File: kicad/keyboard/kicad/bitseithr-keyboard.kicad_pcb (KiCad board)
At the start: 4 copper layers, 419 x 206 mm, 100 parts, among them P2 KEYB CONN 1

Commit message: continued keyboard pcb
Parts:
- added U?: SW-TH_EC11E1820402, clholm-kicad-library:SW-TH_EC11E1820402, F.Cu at (396.5, 176.5)
- added U?: SW-TH_EC11E1820402, clholm-kicad-library:SW-TH_EC11E1820402, F.Cu at (396.5, 136.5)
- moved D31 258.1 mm to (136.1, 225.5)
- moved D34 258.1 mm to (136.1, 223.1)
- moved D36 258.1 mm to (135.3, 218.3)
- moved P2 256.3 mm to (93.3, 234.3)
- moved D37 154.4 mm to (208.0, 86.5)
- moved R16 140.5 mm to (209.0, 96.0)
- moved R15 124.3 mm to (220.0, 83.5)
- moved HOLE 7.00 mm to (192.0, 166.0)
- moved HOLE 4.47 mm to (110.0, 129.0)
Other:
- outline, holes or cut-outs redrawn

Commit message: updated control scheme layout
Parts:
- moved U? 121.1 mm to (303.0, 213.5), turned to 180 degrees
- moved U? 65.0 mm to (343.0, 213.5), turned to 180 degrees
- moved HOLE 4.00 mm to (444.5, 110.2)
- moved HOLE 4.00 mm to (294.5, 62.5)
- moved HOLE 4.00 mm to (194.5, 62.5)
- moved HOLE 4.00 mm to (94.5, 62.5)
- moved HOLE 4.00 mm to (444.5, 158.0)
- moved HOLE 4.00 mm to (444.5, 253.5)
- moved HOLE 4.00 mm to (344.5, 253.5)
- moved HOLE 4.00 mm to (244.5, 253.5)
- moved HOLE 4.00 mm to (444.5, 205.8)
- moved HOLE 4.00 mm to (144.5, 253.5)
- moved HOLE 4.00 mm to (344.5, 62.5)
- moved HOLE 4.00 mm to (144.5, 62.5)
- moved HOLE 4.00 mm to (244.5, 62.5)
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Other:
- board size 419 x 206 mm -> 415 x 206 mm

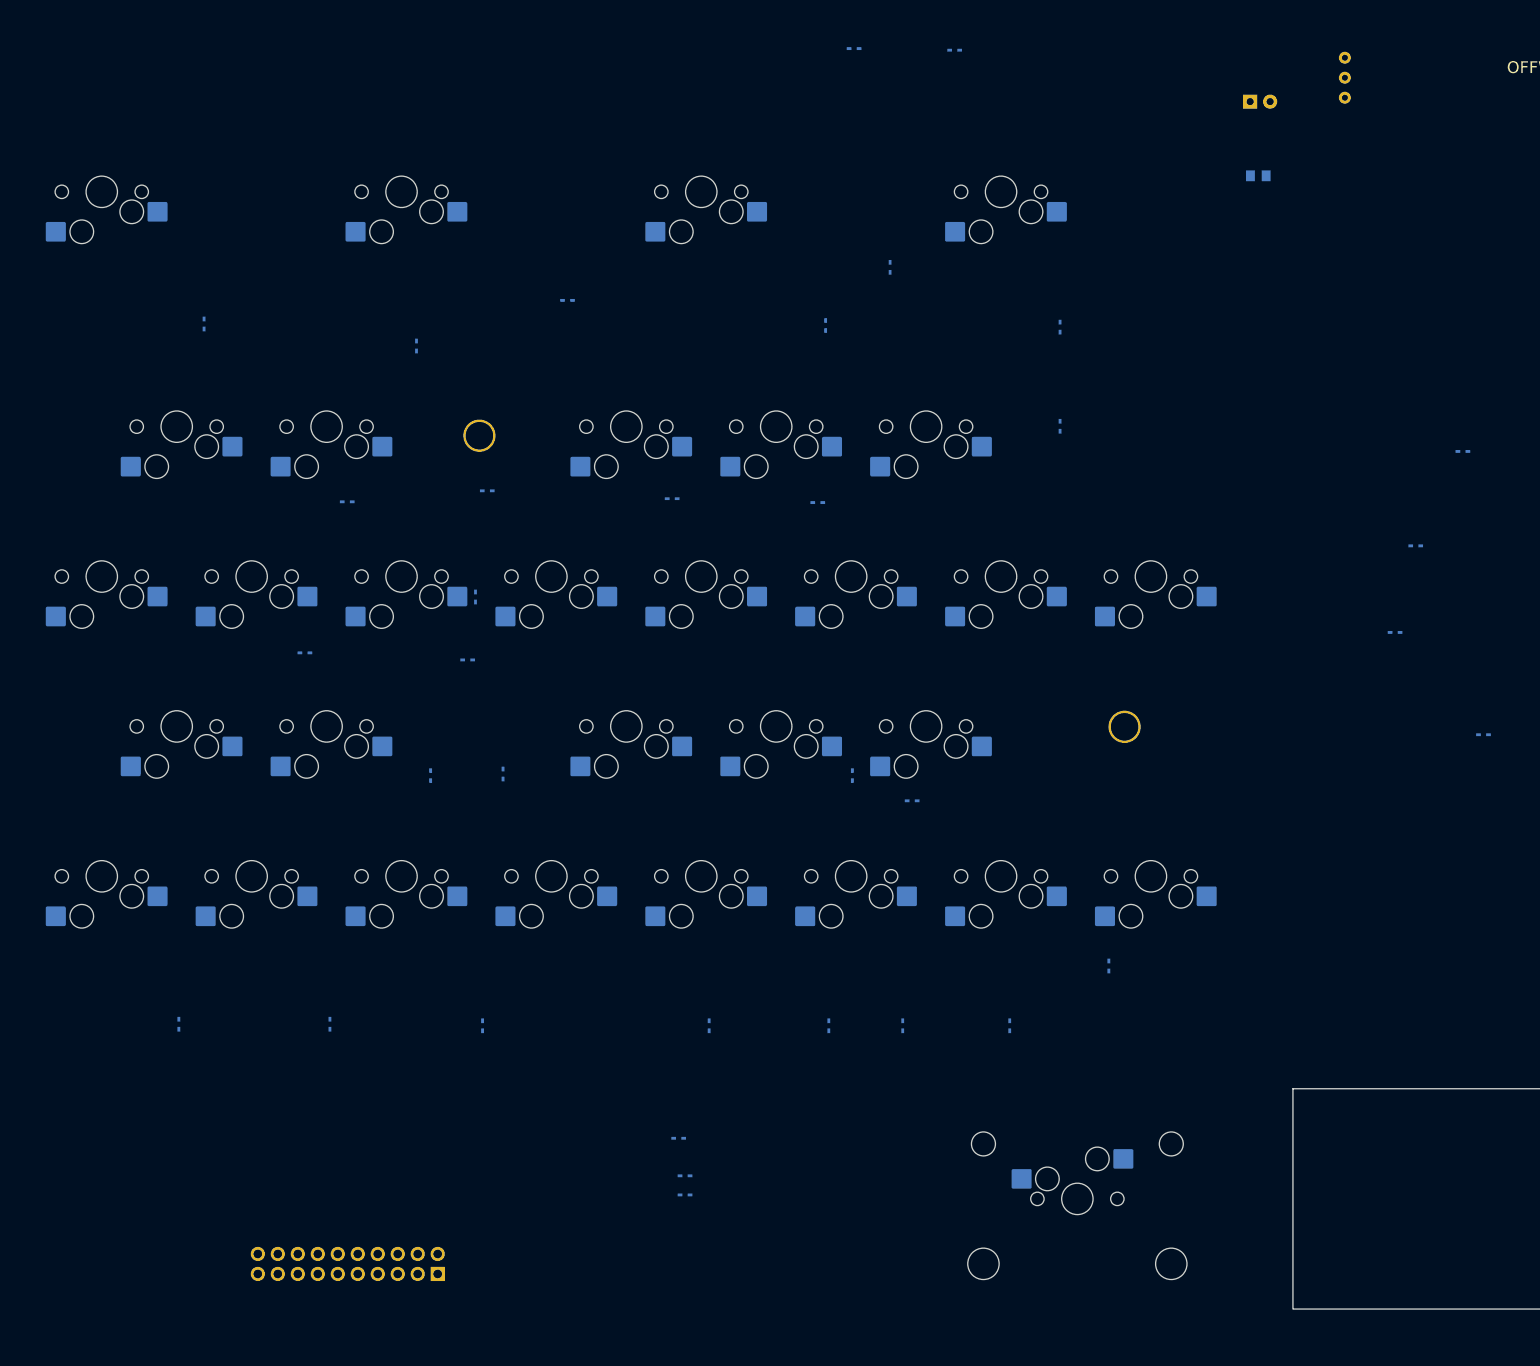
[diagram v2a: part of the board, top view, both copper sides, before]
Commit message: arranged diodes on board
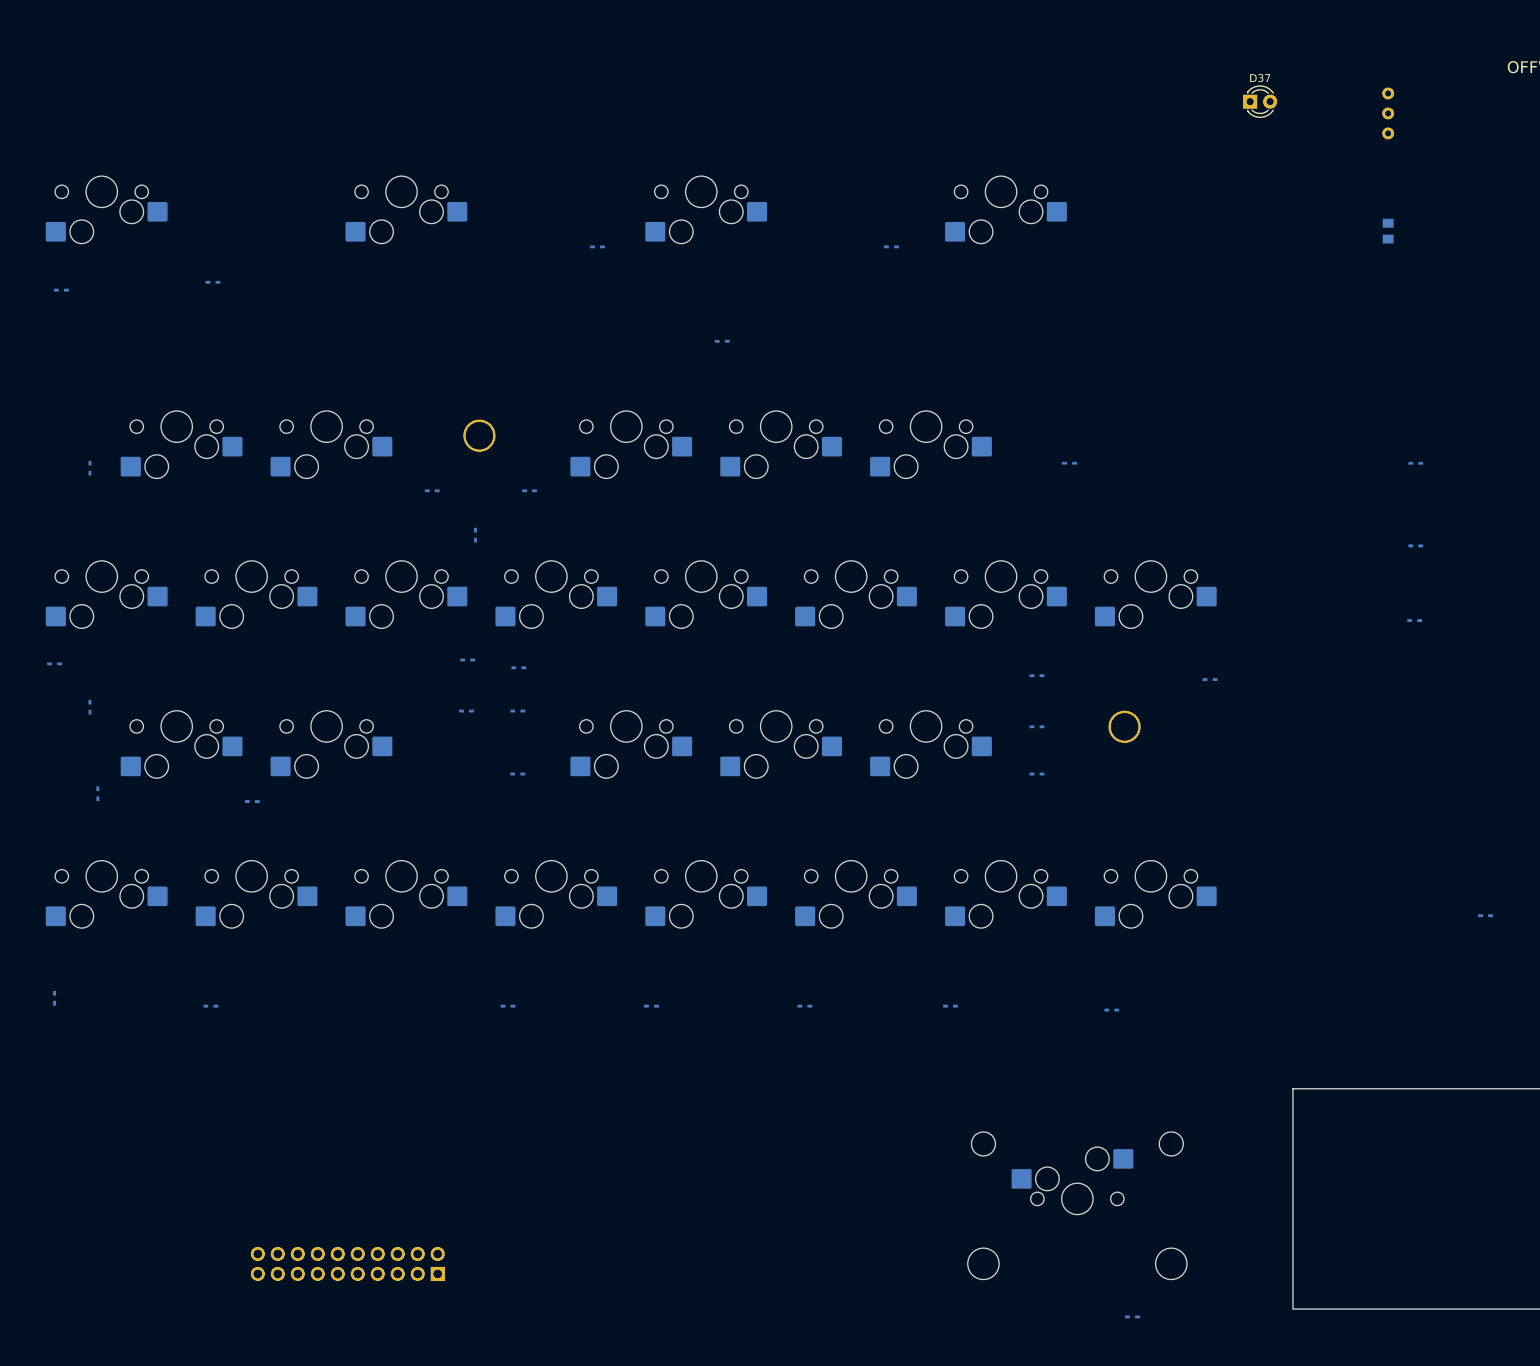
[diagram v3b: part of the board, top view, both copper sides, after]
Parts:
- D37: moved to F.Cu
- moved D16 165.0 mm to (193.0, 241.0)
- moved D25 123.0 mm to (151.4, 201.5), turned to 180 degrees
- moved D34 116.5 mm to (228.9, 152.5)
- moved D36 106.4 mm to (237.9, 190.0)
- moved D10 100.5 mm to (75.9, 201.5)
- moved D21 98.7 mm to (131.9, 201.5), turned to 0 degrees
- moved D6 94.8 mm to (56.0, 200.5), turned to 90 degrees
- moved D31 93.5 mm to (202.9, 160.0)
- moved D32 83.9 mm to (190.4, 202.0)
- moved D15 76.5 mm to (113.6, 201.5), turned to 0 degrees
- moved D30 76.0 mm to (169.9, 201.5), turned to 0 degrees
- moved D24 68.4 mm to (108.4, 164.0), turned to 0 degrees
- moved D12 68.3 mm to (104.0, 136.0), turned to 180 degrees
- moved D11 52.1 mm to (76.1, 109.5), turned to 0 degrees
- moved D14 51.5 mm to (115.0, 158.5), turned to 180 degrees
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
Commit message: shrank board length
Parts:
- moved D37 91.2 mm to (117.9, 72.0)
- moved HOLE 50.0 mm to (394.5, 110.2)
- moved HOLE 50.0 mm to (394.5, 158.0)
- moved HOLE 50.0 mm to (394.5, 253.5)
- moved HOLE 50.0 mm to (394.5, 205.8)
- moved HOLE 50.0 mm to (394.5, 62.5)
- moved HOLE 43.8 mm to (350.8, 253.5)
- moved HOLE 43.8 mm to (350.8, 62.5)
- moved HOLE 37.5 mm to (307.0, 253.5)
- moved HOLE 37.5 mm to (307.0, 62.5)
- moved HOLE 31.2 mm to (263.2, 62.5)
- moved HOLE 31.2 mm to (263.2, 253.5)
- moved HOLE 25.0 mm to (219.5, 253.5)
- moved HOLE 25.0 mm to (219.5, 62.5)
- moved HOLE 18.8 mm to (175.8, 62.5)
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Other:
- board size 415 x 206 mm -> 365 x 206 mm
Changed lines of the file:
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@@
 	(footprint "MountingHole:MountingHole_3.5mm"
 		(layer "F.Cu")
-		(at 444.5 110.25)
+		(at 394.5 110.25)
 		(property "Reference" "HOLE"
 			(at 0 -3.45 0)
@@
 	(footprint "MountingHole:MountingHole_3.5mm"
 		(layer "F.Cu")
-		(at 444.5 205.75)
+		(at 394.5 205.75)
 		(property "Reference" "HOLE"
 			(at 0 -3.45 0)
@@
 	(footprint "MountingHole:MountingHole_3.5mm"
 		(layer "F.Cu")
-		(at 394.5 253.5)
+		(at 350.75 253.5)
 		(property "Reference" "HOLE"
 			(at 0 -3.45 0)
@@
 	(footprint "MountingHole:MountingHole_3.5mm"
 		(layer "F.Cu")
-		(at 294.5 253.5)
+		(at 263.25 253.5)
 		(property "Reference" "HOLE"
 			(at 0 -3.45 0)
@@
 	(footprint "MountingHole:MountingHole_3.5mm"
 		(layer "F.Cu")
-		(at 194.5 253.5)
+		(at 175.75 253.5)
 		(property "Reference" "HOLE"
 			(at 0 -3.45 0)
@@
 	(footprint "MountingHole:MountingHole_3.5mm"
 		(layer "F.Cu")
-		(at 94.5 253.5)
+		(at 88.25 253.5)
 		(property "Reference" "HOLE"
 			(at 0 -3.45 0)
@@
 	(footprint "MountingHole:MountingHole_3.5mm"
 		(layer "F.Cu")
-		(at 394.5 62.5)
+		(at 350.75 62.5)
 		(property "Reference" "HOLE"
 			(at 0 -3.45 0)
@@
 	(footprint "MountingHole:MountingHole_3.5mm"
 		(layer "F.Cu")
-		(at 294.5 62.5)
+		(at 263.25 62.5)
 		(property "Reference" "HOLE"
 			(at 0 -3.45 0)
@@
 	(footprint "MountingHole:MountingHole_3.5mm"
 		(layer "F.Cu")
-		(at 194.5 62.5)
+		(at 175.75 62.5)
 		(property "Reference" "HOLE"
 			(at 0 -3.45 0)
@@
 	(footprint "MountingHole:MountingHole_3.5mm"
 		(layer "F.Cu")
-		(at 94.5 62.5)
+		(at 88.25 62.5)
 		(property "Reference" "HOLE"
 			(at 0 -3.45 0)
@@
 	(footprint "MountingHole:MountingHole_5.7mm"
 		(layer "F.Cu")
-		(at 444.5 158)
+		(at 394.5 158)
 		(property "Reference" "HOLE"
 			(at 0 -3.45 0)
@@
 	(footprint "MountingHole:MountingHole_5.7mm"
 		(layer "F.Cu")
-		(at 444.5 253.5)
+		(at 394.5 253.5)
 		(property "Reference" "HOLE"
 			(at 0 -3.45 0)
@@
 	(footprint "MountingHole:MountingHole_5.7mm"
 		(layer "F.Cu")
-		(at 344.5 253.5)
+		(at 307 253.5)
 		(property "Reference" "HOLE"
 			(at 0 -3.45 0)
@@
 	(footprint "MountingHole:MountingHole_5.7mm"
 		(layer "F.Cu")
-		(at 244.5 253.5)
+		(at 219.5 253.5)
 		(property "Reference" "HOLE"
 			(at 0 -3.45 0)
@@
 	(footprint "MountingHole:MountingHole_5.7mm"
 		(layer "F.Cu")
-		(at 144.5 253.5)
+		(at 132 253.5)
 		(property "Reference" "HOLE"
 			(at 0 -3.45 0)
@@
 	(footprint "MountingHole:MountingHole_5.7mm"
 		(layer "F.Cu")
-		(at 344.5 62.5)
+		(at 307 62.5)
 		(property "Reference" "HOLE"
 			(at 0 -3.45 0)
@@
 	(footprint "MountingHole:MountingHole_5.7mm"
 		(layer "F.Cu")
-		(at 144.5 62.5)
+		(at 132 62.5)
 		(property "Reference" "HOLE"
 			(at 0 -3.45 0)
@@
 	(footprint "MountingHole:MountingHole_5.7mm"
 		(layer "F.Cu")
-		(at 244.5 62.5)
+		(at 219.5 62.5)
 		(property "Reference" "HOLE"
 			(at 0 -3.45 0)
@@
 	(footprint "MountingHole:MountingHole_5.7mm"
 		(layer "F.Cu")
-		(at 444.5 62.5)
+		(at 394.5 62.5)
 		(property "Reference" "HOLE"
 			(at 0 -3.45 0)
@@
 	(footprint "LED_THT:LED_D3.0mm"
 		(layer "F.Cu")
-		(at 207.96 86.54)
+		(at 117.88 72)
 		(descr "LED, diameter 3.0mm, 2 pins, generated by kicad-footprint-generator")
 		(tags "LED")
@@
 	(footprint "EasyEDA_Lib:RES-ADJ-TH_3296W"
 		(layer "B.Cu")
-		(at 225.5 88.04)
+		(at 210.04 85.5 90)
 		(property "Reference" "R15"
-			(at -0.04275 5.795433 180)
+			(at -0.04275 5.795433 90)
 			(layer "B.SilkS")
 			(effects
@@
 		)
 		(property "Value" "1kΩ"
-			(at -0.04275 -5.7655 180)
+			(at -0.04275 -5.7655 90)
 			(layer "B.Fab")
 			(effects
@@
 		)
 		(property "Datasheet" "https://item.szlcsc.com/datasheet/3296W-1-102LF/58119.html"
-			(at 0 0 180)
+			(at 0 0 90)
 			(layer "B.Fab")
 			(hide yes)
@@
 		)
 		(property "Description" "Resistance:1kΩ Tolerance:±10% Tolerance:±10% Power(Watts):500mW Temperature Coefficient:±100ppm/°C Temperature Coefficient:±100ppm/°C Number of Turns:"
-			(at 0 0 180)
+			(at 0 0 90)
 			(layer "B.Fab")
 			(hide yes)
@@
 		)
 		(property "JLC_3DModel_Q" "d75c81813a0c4fc5896bd8a59ffd69dd"
-			(at 0 0 180)
+			(at 0 0 90)
 			(layer "Cmts.User")
 			(hide yes)
@@
 		)
 		(property "JLC_3D_Size" "9.5 4.8"
-			(at 0 0 180)
+			(at 0 0 90)
 			(layer "Cmts.User")
 			(hide yes)
@@
 		)
 		(property "Manufacturer Part" "3296W-1-102LF"
-			(at 0 0 180)
+			(at 0 0 270)
 			(unlocked yes)
 			(layer "B.Fab")
@@
 		)
 		(property "Manufacturer" "BOURNS"
-			(at 0 0 180)
+			(at 0 0 270)
 			(unlocked yes)
 			(layer "B.Fab")
@@
 		)
 		(property "Supplier Part" "C57089"
-			(at 0 0 180)
+			(at 0 0 270)
 			(unlocked yes)
 			(layer "B.Fab")
@@
 		)
 		(property "Supplier" "LCSC"
-			(at 0 0 180)
+			(at 0 0 270)
 			(unlocked yes)
 			(layer "B.Fab")
@@
 		)
 		(property "LCSC Part Name" "1kΩ ±10%"
-			(at 0 0 180)
+			(at 0 0 270)
 			(unlocked yes)
 			(layer "B.Fab")
@@
 		(sheetfile "bitseithr-keyboard.kicad_sch")
 		(fp_line
-			(start -2.734 -4.826)
-			(end -2.734 4.826)
+			(start 2.6 -4.826)
+			(end -2.734 -4.826)
 			(stroke
 				(width 0.254)
@@
 		)
 		(fp_line
-			(start -2.734 4.826)
-			(end 2.6 4.826)
+			(start -2.734 -4.826)
+			(end -2.734 4.826)
 			(stroke
 				(width 0.254)
@@
 		)
 		(fp_line
-			(start -2.58 -4.75)
-			(end -2.58 -3.988)
+			(start -2.38 -4.75)
+			(end -2.58 -4.75)
 			(stroke
 				(width 0.254)
@@
 		)
 		(fp_line
-			(start -2.58 -3.988)
-			(end -2.38 -3.988)
+			(start -2.58 -4.75)
+			(end -2.58 -3.988)
 			(stroke
 				(width 0.254)
@@
 		)
 		(fp_line
-			(start -2.58 3.988)
-			(end -2.58 4.75)
+			(start -2.38 -3.988)
+			(end -2.38 -4.75)
 			(stroke
 				(width 0.254)
@@
 		)
 		(fp_line
-			(start -2.58 4.75)
-			(end -2.38 4.75)
+			(start -2.58 -3.988)
+			(end -2.38 -3.988)
 			(stroke
 				(width 0.254)
@@
 		)
 		(fp_line
-			(start -2.38 -4.75)
-			(end -2.58 -4.75)
+			(start 2.092 2.804)
+			(end 1.711 2.804)
 			(stroke
 				(width 0.254)
@@
 		)
 		(fp_line
-			(start -2.38 -3.988)
-			(end -2.38 -4.75)
+			(start 1.711 2.804)
+			(end 2.092 2.804)
 			(stroke
 				(width 0.254)
@@
 		)
 		(fp_line
-			(start -2.38 3.988)
-			(end -2.58 3.988)
+			(start 1.33 2.804)
+			(end 1.711 2.804)
 			(stroke
 				(width 0.254)
@@
 		)
 		(fp_line
-			(start -2.38 4.75)
-			(end -2.38 3.988)
+			(start -2.38 3.988)
+			(end -2.58 3.988)
 			(stroke
 				(width 0.254)
@@
 		)
 		(fp_line
-			(start 1.33 2.804)
-			(end 1.711 2.804)
+			(start -2.58 3.988)
+			(end -2.58 4.75)
 			(stroke
 				(width 0.254)
@@
 		)
 		(fp_line
-			(start 1.711 2.804)
-			(end 2.092 2.804)
+			(start -2.38 4.75)
+			(end -2.38 3.988)
 			(stroke
 				(width 0.254)
@@
 		)
 		(fp_line
-			(start 2.092 2.804)
-			(end 1.711 2.804)
+			(start -2.58 4.75)
+			(end -2.38 4.75)
 			(stroke
 				(width 0.254)
@@
 		)
 		(fp_line
-			(start 2.6 -4.826)
-			(end -2.734 -4.826)
+			(start 2.6 4.826)
+			(end 2.6 -4.826)
 			(stroke
 				(width 0.254)
@@
 		)
 		(fp_line
-			(start 2.6 4.826)
-			(end 2.6 -4.826)
+			(start -2.734 4.826)
+			(end 2.6 4.826)
 			(stroke
 				(width 0.254)
@@
 		)
 		(fp_line
-			(start -2.355 -4.765)
-			(end -2.355 4.765)
+			(start 2.475 -4.765)
+			(end -2.355 -4.765)
 			(stroke
 				(width 0.051)
@@
 		)
 		(fp_line
-			(start -2.355 4.765)
-			(end 2.475 4.765)
+			(start -2.355 -4.765)
+			(end -2.355 4.765)
 			(stroke
 				(width 0.051)
@@
 		)
 		(fp_line
-			(start 2.475 -4.765)
-			(end -2.355 -4.765)
+			(start 2.475 4.765)
+			(end 2.475 -4.765)
 			(stroke
 				(width 0.051)
@@
 		)
 		(fp_line
-			(start 2.475 4.765)
-			(end 2.475 -4.765)
+			(start -2.355 4.765)
+			(end 2.475 4.765)
 			(stroke
 				(width 0.051)
@@
 		)
 		(fp_text user "${REFERENCE}"
-			(at 0 0 180)
+			(at 0 0 90)
 			(layer "B.Fab")
 			(effects
@@
 		)
 		(pad "1" thru_hole circle
-			(at 0 2.54 90)
+			(at 0 2.54 180)
 			(size 1.524 1.524)
 			(drill 0.762)
@@
 		)
 		(pad "2" thru_hole circle
-			(at 0 0 90)
+			(at 0 0 180)
 			(size 1.524 1.524)
 			(drill 0.762)
@@
 		)
 		(pad "3" thru_hole circle
-			(at 0 -2.54 90)
+			(at 0 -2.54 180)
 			(size 1.524 1.524)
 			(drill 0.762)
@@
 	)
 	(gr_line
-		(start 452 261)
+		(start 402 261)
 		(end 37 261)
 		(stroke
@@
 	)
 	(gr_line
-		(start 452 55)
-		(end 452 261)
+		(start 402 55)
+		(end 402 261)
 		(stroke
 			(width 0.1)
@@
 	(gr_line
 		(start 37 55)
-		(end 452 55)
+		(end 402 55)
 		(stroke
 			(width 0.1)

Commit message: moved some diodes around
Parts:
- moved D13 63.9 mm to (94.5, 196.0), turned to 90 degrees
- moved D35 30.6 mm to (241.4, 171.0)
- moved D16 25.9 mm to (192.0, 215.1), turned to -90 degrees
- moved D7 22.8 mm to (102.5, 135.5)
- moved D12 22.6 mm to (101.6, 158.5), turned to 0 degrees
- moved D11 17.8 mm to (93.9, 108.5)
- moved R16 13.9 mm to (212.5, 98.0)
- moved D31 13.6 mm to (189.5, 157.5)
- moved D24 13.5 mm to (117.5, 174.0)
- moved D34 12.6 mm to (241.5, 152.0)
- moved D33 12.4 mm to (241.4, 133.0)
- moved D26 8.73 mm to (170.4, 108.5)
- moved D28 8.54 mm to (177.9, 158.0)
- moved D17 7.95 mm to (132.1, 108.5), turned to 0 degrees
- moved D27 7.20 mm to (177.9, 133.5), turned to 180 degrees
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
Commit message: fixed unclosed inner cutout, began key matrix traces
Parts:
- added HOLE: M3-hole, MountingHole:MountingHole_3.5mm, F.Cu at (267.8, 212.5)
- added HOLE: M3-hole, MountingHole:MountingHole_3.5mm, F.Cu at (263.2, 100.0)
- added HOLE: M3-hole, MountingHole:MountingHole_3.5mm, F.Cu at (289.0, 166.0)
- moved P2 16.9 mm to (98.6, 218.2), turned to 180 degrees
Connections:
- P2 pad 1: +9V -> COL0
- P2 pad 10: COL1 -> ROW4
- P2 pad 11: COL2 -> COL5
- P2 pad 12: COL3 -> ROW5
- P2 pad 13: COL4 -> COL6
- P2 pad 14: COL5 -> unconnected-(P2-Pad14)
- P2 pad 15: COL6 -> COL7
- P2 pad 16: COL7 -> unconnected-(P2-Pad16)
- P2 pad 18: unconnected-(P2-Pad18) -> GND
- P2 pad 2: GND -> ROW0
- P2 pad 20: unconnected-(P2-Pad20) -> +9V
- P2 pad 3: ROW0 -> COL1
- P2 pad 5: ROW2 -> COL2
- P2 pad 6: ROW3 -> ROW2
- P2 pad 7: ROW4 -> COL3
- P2 pad 8: ROW5 -> ROW3
- P2 pad 9: COL0 -> COL4
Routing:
- net ROW1: track 0.00 -> 675.5 mm, vias 0 -> 6
- net ROW2: track 0.00 -> 442.8 mm, vias 0 -> 2
- net ROW3: track 0.00 -> 333.2 mm, vias 0 -> 1
- net ROW0: track 0.00 -> 276.1 mm, vias 0 -> 4
- net ROW4: track 0.00 -> 212.1 mm, vias 0 -> 1
- net ROW5: track 0.00 -> 136.5 mm, vias 0 -> 1
- net Net-(D23-A): track 0.00 -> 40.8 mm, vias 0 -> 2
- net Net-(D27-A): track 0.00 -> 19.8 mm
- net Net-(D7-A): track 0.00 -> 18.2 mm
- net Net-(D18-A): track 0.00 -> 17.2 mm
- net Net-(D22-A): track 0.00 -> 16.2 mm
- net Net-(D28-A): track 0.00 -> 10.1 mm
- net Net-(D31-A): track 0.00 -> 5.78 mm
- net Net-(D26-A): track 0.00 -> 5.64 mm
- net Net-(D17-A): track 0.00 -> 5.59 mm
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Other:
- outline, holes or cut-outs redrawn
